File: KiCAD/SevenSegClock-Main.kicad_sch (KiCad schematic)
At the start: 0 parts

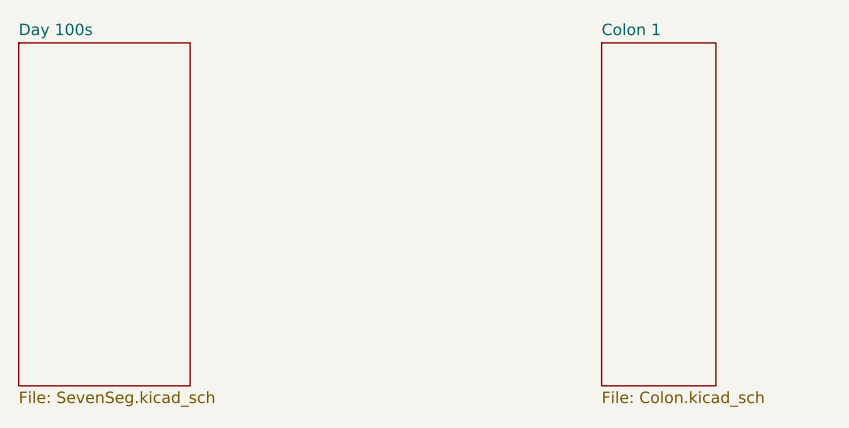
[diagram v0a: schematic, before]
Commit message: Initial PCB layout for 7-seg digits
I realize now that the PCB for the digits needs to be slanted, otherwise the colon pcb won't fit next to it, grumble
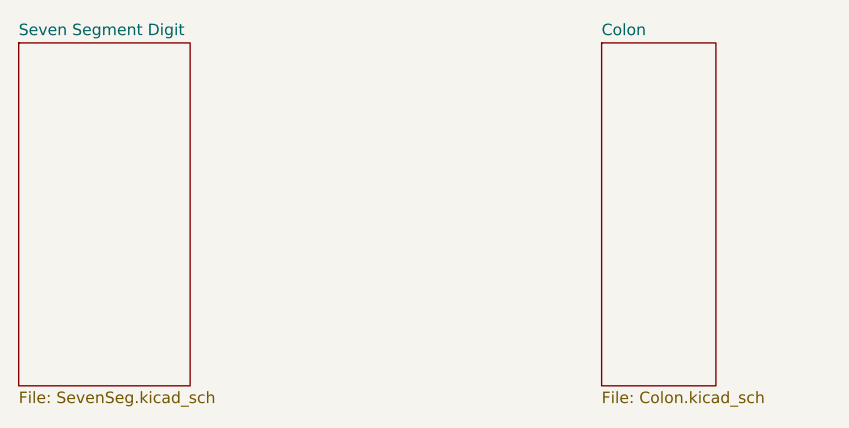
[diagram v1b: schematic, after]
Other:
- sheet Colon 1 renamed Colon
- sheet Day 100s renamed Seven Segment Digit
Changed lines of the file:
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@@
     (stroke (width 0.1524) (type solid))
     (fill (color 255 255 194 1.0000))
-    (property "Sheetname" "Colon 1" (at 133.35 128.8284 0)
+    (property "Sheetname" "Colon" (at 133.35 128.8284 0)
       (effects (font (size 1.27 1.27)) (justify left bottom))
     )
@@
     (stroke (width 0.1524) (type solid))
     (fill (color 255 255 194 1.0000))
-    (property "Sheetname" "Day 100s" (at 68.58 128.8284 0)
+    (property "Sheetname" "Seven Segment Digit" (at 68.58 128.8284 0)
       (effects (font (size 1.27 1.27)) (justify left bottom))
     )
